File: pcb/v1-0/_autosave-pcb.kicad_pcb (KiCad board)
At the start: 2 copper layers, 254 x 40.6 mm, 124 parts, among them J1 Conn_01x04, J3 Conn_01x01, J4 Conn_01x01, J5 Conn_01x02, J6 Conn_01x04, J7 10118194-0001LF, J8 Conn_02x03_Odd_Even, U1 ATtiny3216-S, U2 SI7211-B-00-IV

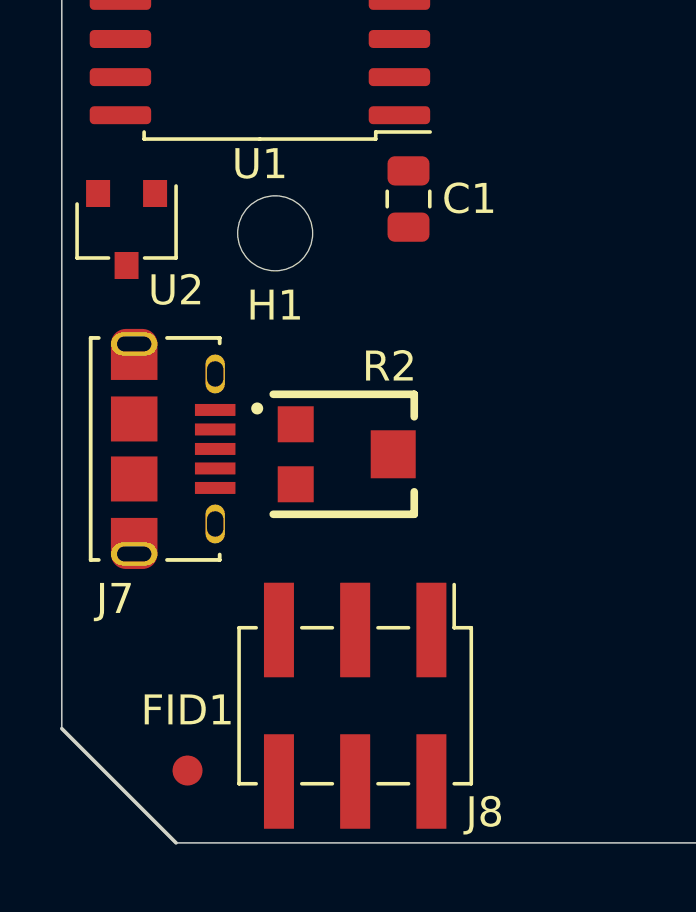
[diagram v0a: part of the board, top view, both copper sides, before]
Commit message: consider program over custom USB and remove 100 mil UPDI header
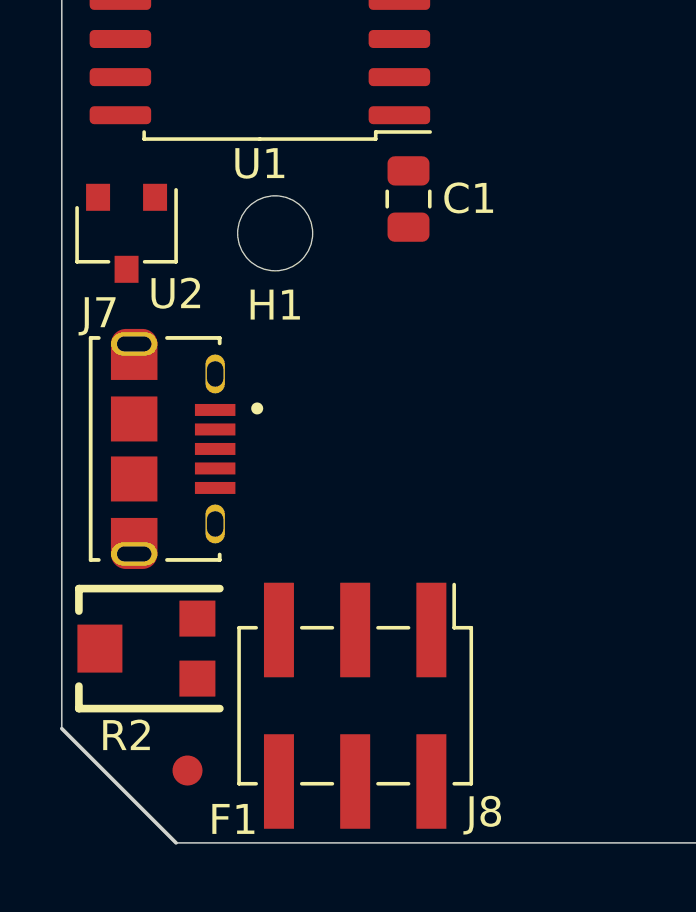
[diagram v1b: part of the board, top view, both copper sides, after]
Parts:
- moved R2 9.16 mm to (28.3, 110.4), turned to 90 degrees
- moved U2 0.13 mm to (27.6, 96.5)
- renumbered FID1 to F1, Je to J2
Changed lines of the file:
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@@
     (descr "Through hole straight pin header, 1x01, 2.54mm pitch, single row")
     (tags "Through hole pin header THT 1x01 2.54mm single row")
-    (fp_text reference Je (at 0 2.33) (layer B.SilkS)
+    (fp_text reference J2 (at 0 2.33) (layer B.SilkS)
       (effects (font (size 1 1) (thickness 0.15)) (justify mirror))
     )
@@
       (effects (font (size 1 1) (thickness 0.15)) (justify mirror))
     )
+    (fp_line (start -0.635 1.27) (end 1.27 1.27) (layer B.Fab) (width 0.1))
+    (fp_line (start 1.27 1.27) (end 1.27 -1.27) (layer B.Fab) (width 0.1))
+    (fp_line (start 1.27 -1.27) (end -1.27 -1.27) (layer B.Fab) (width 0.1))
+    (fp_line (start -1.27 -1.27) (end -1.27 0.635) (layer B.Fab) (width 0.1))
+    (fp_line (start -1.27 0.635) (end -0.635 1.27) (layer B.Fab) (width 0.1))
+    (fp_line (start -1.33 -1.33) (end 1.33 -1.33) (layer B.SilkS) (width 0.12))
+    (fp_line (start -1.33 -1.27) (end -1.33 -1.33) (layer B.SilkS) (width 0.12))
+    (fp_line (start 1.33 -1.27) (end 1.33 -1.33) (layer B.SilkS) (width 0.12))
+    (fp_line (start -1.33 -1.27) (end 1.33 -1.27) (layer B.SilkS) (width 0.12))
+    (fp_line (start -1.33 0) (end -1.33 1.33) (layer B.SilkS) (width 0.12))
+    (fp_line (start -1.33 1.33) (end 0 1.33) (layer B.SilkS) (width 0.12))
+    (fp_line (start -1.8 1.8) (end -1.8 -1.8) (layer B.CrtYd) (width 0.05))
+    (fp_line (start -1.8 -1.8) (end 1.8 -1.8) (layer B.CrtYd) (width 0.05))
+    (fp_line (start 1.8 -1.8) (end 1.8 1.8) (layer B.CrtYd) (width 0.05))
+    (fp_line (start 1.8 1.8) (end -1.8 1.8) (layer B.CrtYd) (width 0.05))
     (fp_text user %R (at 0 0 -90) (layer B.Fab)
       (effects (font (size 1 1) (thickness 0.15)) (justify mirror))
     )
-    (fp_line (start 1.8 1.8) (end -1.8 1.8) (layer B.CrtYd) (width 0.05))
-    (fp_line (start 1.8 -1.8) (end 1.8 1.8) (layer B.CrtYd) (width 0.05))
-    (fp_line (start -1.8 -1.8) (end 1.8 -1.8) (layer B.CrtYd) (width 0.05))
-    (fp_line (start -1.8 1.8) (end -1.8 -1.8) (layer B.CrtYd) (width 0.05))
-    (fp_line (start -1.33 1.33) (end 0 1.33) (layer B.SilkS) (width 0.12))
-    (fp_line (start -1.33 0) (end -1.33 1.33) (layer B.SilkS) (width 0.12))
-    (fp_line (start -1.33 -1.27) (end 1.33 -1.27) (layer B.SilkS) (width 0.12))
-    (fp_line (start 1.33 -1.27) (end 1.33 -1.33) (layer B.SilkS) (width 0.12))
-    (fp_line (start -1.33 -1.27) (end -1.33 -1.33) (layer B.SilkS) (width 0.12))
-    (fp_line (start -1.33 -1.33) (end 1.33 -1.33) (layer B.SilkS) (width 0.12))
-    (fp_line (start -1.27 0.635) (end -0.635 1.27) (layer B.Fab) (width 0.1))
-    (fp_line (start -1.27 -1.27) (end -1.27 0.635) (layer B.Fab) (width 0.1))
-    (fp_line (start 1.27 -1.27) (end -1.27 -1.27) (layer B.Fab) (width 0.1))
-    (fp_line (start 1.27 1.27) (end 1.27 -1.27) (layer B.Fab) (width 0.1))
-    (fp_line (start -0.635 1.27) (end 1.27 1.27) (layer B.Fab) (width 0.1))
     (pad 1 thru_hole rect (at 0 0) (size 1.7 1.7) (drill 1) (layers *.Cu *.Mask)
       (net 20 RxD))
@@
   )
   (module Package_TO_SOT_SMD:SC-59 (layer F.Cu)
-    (at 27.559 96.393 270)
+    (at 27.559 96.52 270)
     (descr "SC-59, https://lib.chipdip.ru/images/import_diod/original/SOT-23_SC-59.jpg")
     (tags SC-59)
@@
   )
   (module TC33X-2-103E:35WR (layer F.Cu)
-    (at 34.798 103.886 270)
-    (fp_text reference R2 (at -2.921 -1.524) (layer F.SilkS)
+    (at 28.32 110.363 90)
+    (fp_text reference R2 (at -2.921 -0.761) (layer F.SilkS)
       (effects (font (size 1.001276 1.001276) (thickness 0.15)))
     )
@@
     (fp_line (start -2 -2.35) (end -2 2.35) (layer F.Fab) (width 0.254))
     (fp_line (start 2 -2.35) (end -2 -2.35) (layer F.Fab) (width 0.254))
-    (pad 2 smd rect (at 0 -1.65 270) (size 1.6 1.5) (layers F.Cu F.Paste F.Mask)
+    (pad 2 smd rect (at 0 -1.65 90) (size 1.6 1.5) (layers F.Cu F.Paste F.Mask)
       (net 30 BRIGHTNESS))
-    (pad 3 smd rect (at 1 1.6 270) (size 1.2 1.2) (layers F.Cu F.Paste F.Mask)
+    (pad 3 smd rect (at 1 1.6 90) (size 1.2 1.2) (layers F.Cu F.Paste F.Mask)
       (net 13 GND))
-    (pad 1 smd rect (at -1 1.6 270) (size 1.2 1.2) (layers F.Cu F.Paste F.Mask)
+    (pad 1 smd rect (at -1 1.6 90) (size 1.2 1.2) (layers F.Cu F.Paste F.Mask)
       (net 14 +5V))
     (model ${KIPRJMOD}/lib/TC33X-2-103E/TC33X-2-103G--3DModel-STEP-1.STEP
@@
   (module microUSB:AMPHENOL_10118194-0001LF (layer F.Cu)
     (at 27.813 103.7082 270)
-    (fp_text reference J7 (at 5.0038 0.635 180) (layer F.SilkS)
+    (fp_text reference J7 (at -4.5212 1.143 180) (layer F.SilkS)
       (effects (font (size 1.000953 1.000953) (thickness 0.15)))
     )
@@
     (tags fiducial)
     (attr smd)
-    (fp_text reference FID1 (at 0 -2) (layer F.SilkS)
-      (effects (font (size 1 1) (thickness 0.15)))
-    )
+    (fp_text reference F1 (at 1.524 1.651) (layer F.SilkS)
+      (effects (font (size 1 1) (thickness 0.15)))
+    )
